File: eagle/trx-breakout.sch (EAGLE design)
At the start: 17 parts, among them J1 DF12NB(3.0)-10DX-0.5VHRS_DF12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, Q1 BSS84, Q2 BSS84, Q3 BSS123, Q4 BSS123

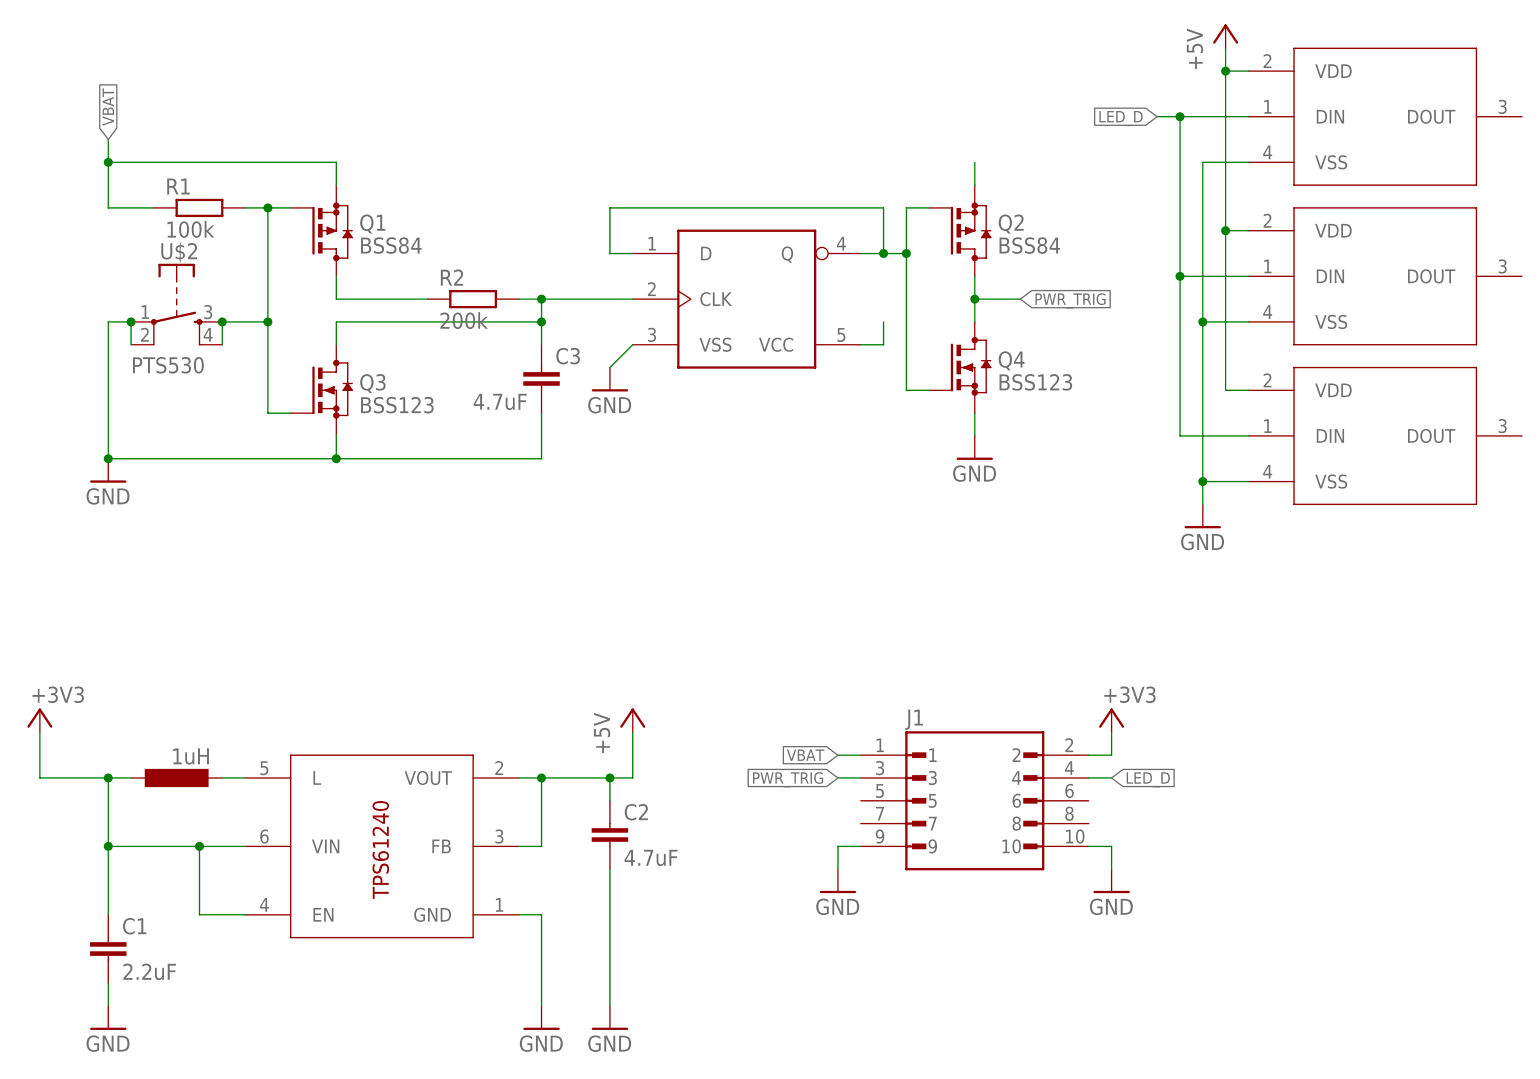
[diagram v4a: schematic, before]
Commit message: Designed new boards wit fixed errors
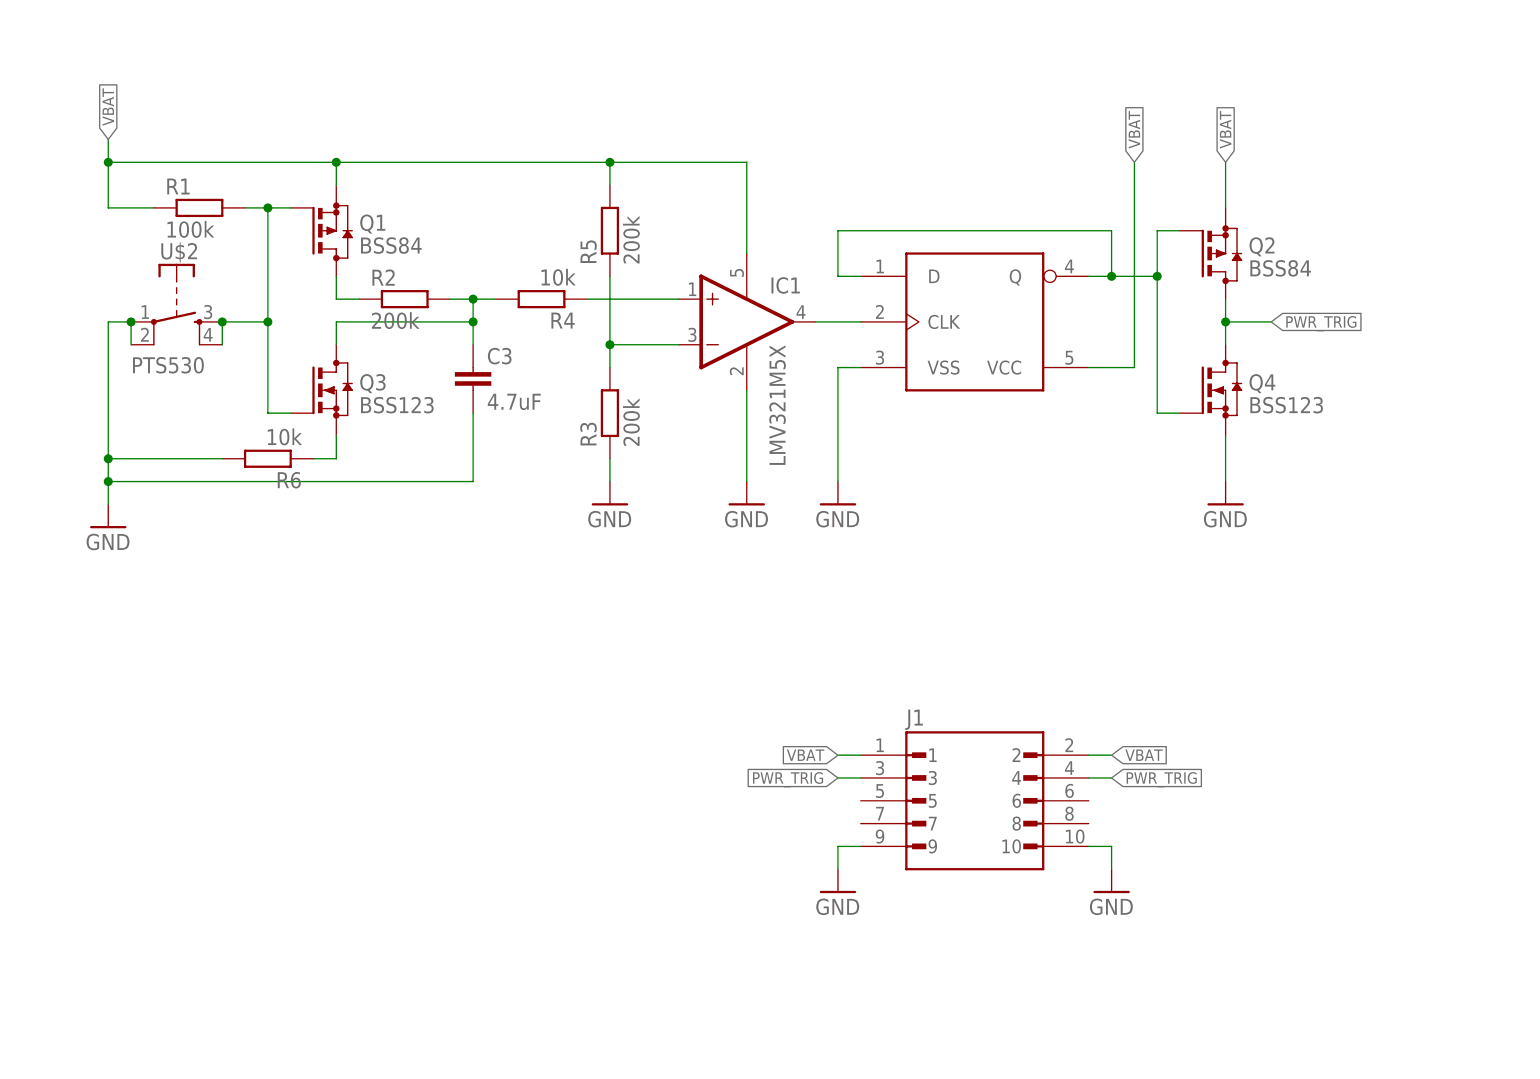
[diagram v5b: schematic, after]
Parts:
- removed C1: 2.2uF, rcl:C-EUC0805
- removed C2: 4.7uF, rcl:C-EUC0805
- removed U$3: TPS61240, texas-instruments:TPS61240
- removed U$4: 1uH, inductor-vishay:IHLP-1212
- removed U$5, U$6, U$7: ARGB_LED, led:ARGB_LED
- added IC1: LMV321M5X, linear:LMV321M5X
- added R3, R5: 200k, rcl:R-EU_R0805
- added R4, R6: 10k, rcl:R-EU_R0805
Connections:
- removed net +3V3: C1.1, J1.2, U$3.EN, U$3.VIN, U$4.1
- removed net +5V: C2.1, U$3.FB, U$3.VOUT, U$5.VDD, U$6.VDD, U$7.VDD
- removed net LED_D: J1.4, U$5.DIN, U$6.DIN, U$7.DIN
- new net N$8: Q3.S, R6.1
- net GND: now also IC1.V-, R3.1, R6.2; no longer C1.2, C2.2, Q3.S, U$3.GND, U$5.VSS, U$6.VSS, U$7.VSS
- net N$1: now also IC1.-IN, R3.2, R5.1; no longer U$3.L, U$4.2
- net N$3: now also R4.2; no longer U$1.CLK
- net N$6: now also IC1.+IN, R4.1; no longer U$1.VCC
- net N$7: now also IC1.OUT, U$1.CLK; no longer Q2.S
- net PWR_TRIG: now also J1.4
- net VBAT: now also IC1.V+, J1.2, Q2.S, R5.2, U$1.VCC
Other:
- moved on the sheet: C3, Q2, Q4, R2

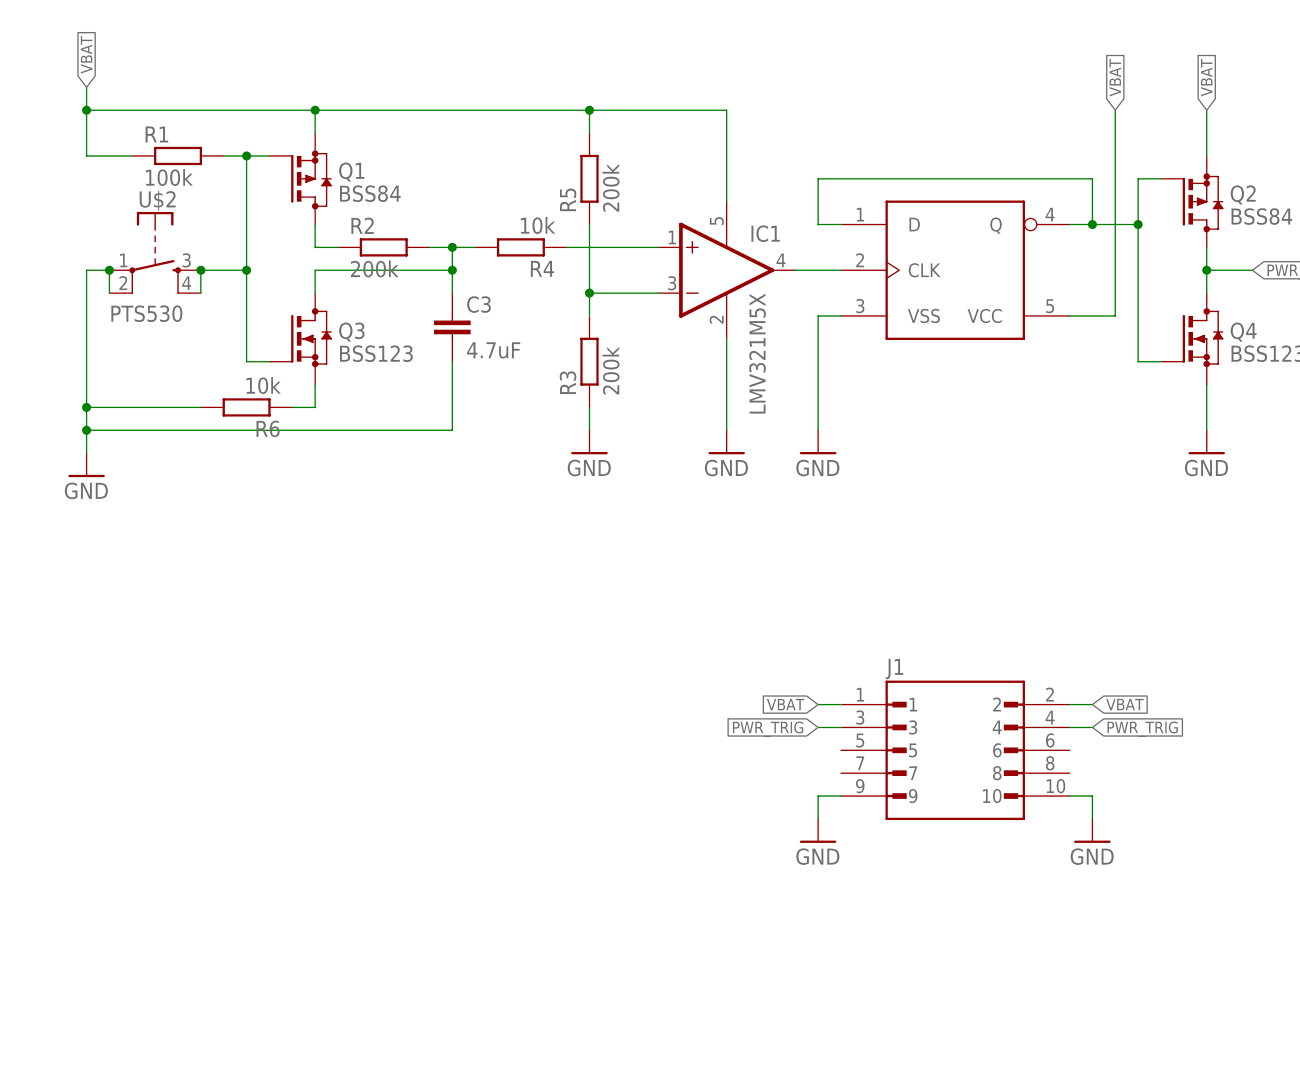
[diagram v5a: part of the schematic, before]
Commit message: Reworked breakout board
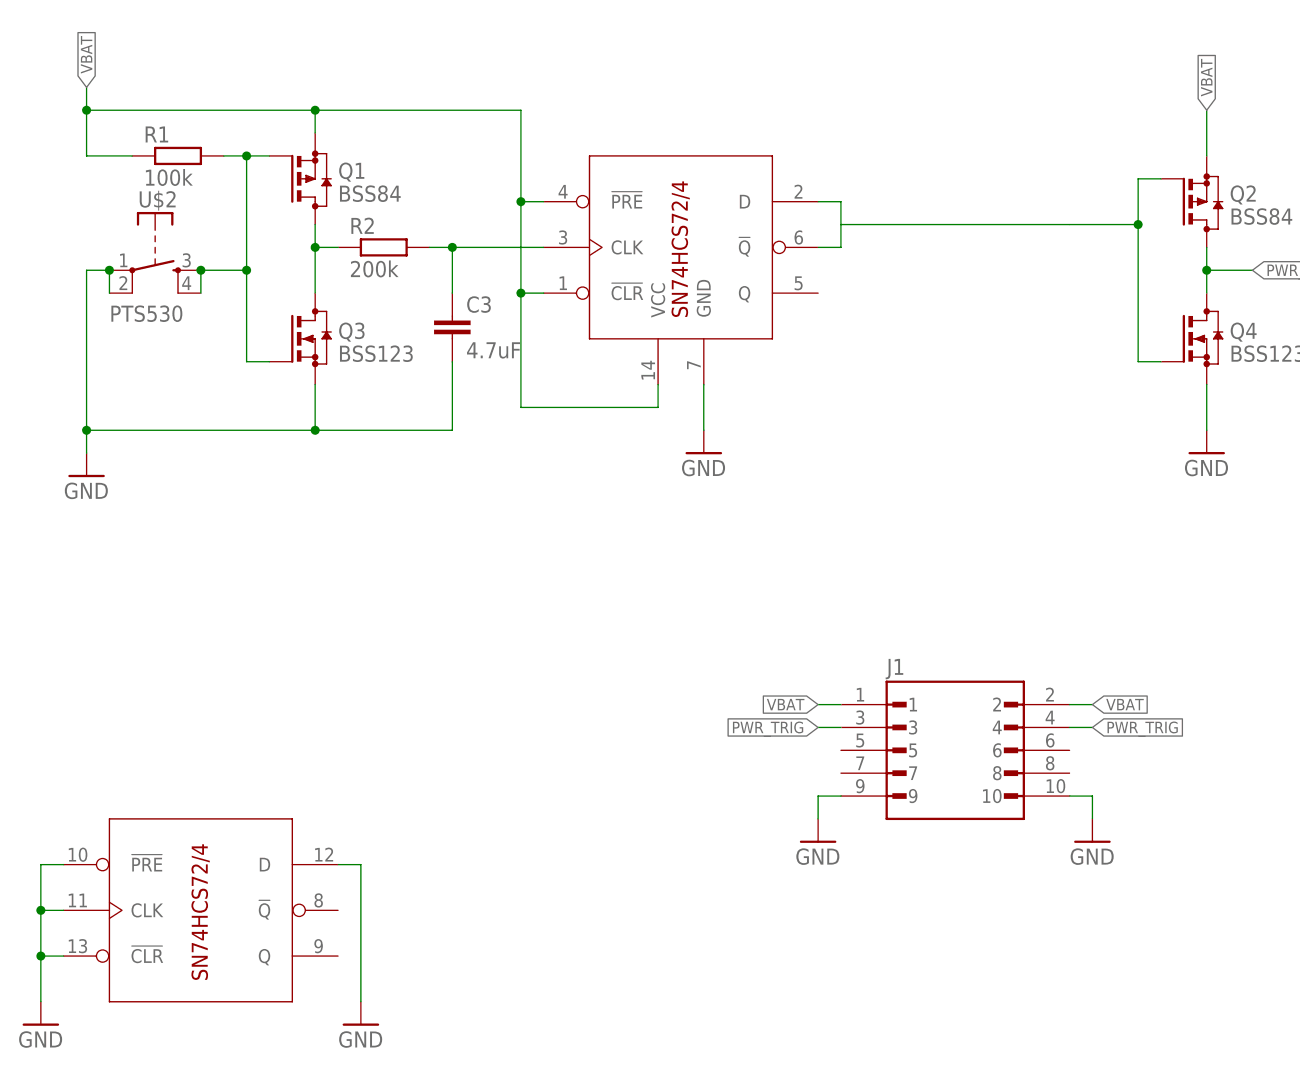
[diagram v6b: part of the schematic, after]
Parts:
- removed IC1: LMV321M5X, linear:LMV321M5X
- removed R3, R5: 200k, rcl:R-EU_R0805
- removed R4, R6: 10k, rcl:R-EU_R0805
- U$1: value SN74LVC1G80 -> SN74HCS72/4; device texas-instruments:SN74LVC1G80 -> texas-instruments:SN74HCS72/4
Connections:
- removed net N$6: IC1.+IN, R4.1
- removed net N$7: IC1.OUT, U$1.CLK
- removed net N$8: Q3.S, R6.1
- net GND: now also Q3.S, U$1G2.!CLR, U$1G2.!PRE, U$1G2.CLK, U$1G2.D, U$1SUPPPLY.GND; no longer IC1.V-, R3.1, R6.2, U$1.VSS
- net N$1: now also Q1.D, Q3.D, R2.1; no longer IC1.-IN, R3.2, R5.1
- net N$2: now also U$1G1.!Q, U$1G1.D; no longer Q1.D, R2.1
- net N$3: now also U$1G1.CLK; no longer Q3.D, R4.2
- net N$5: no longer U$1.D, U$1.Q
- net VBAT: now also U$1G1.!CLR, U$1G1.!PRE, U$1SUPPPLY.VCC; no longer IC1.V+, R5.2, U$1.VCC

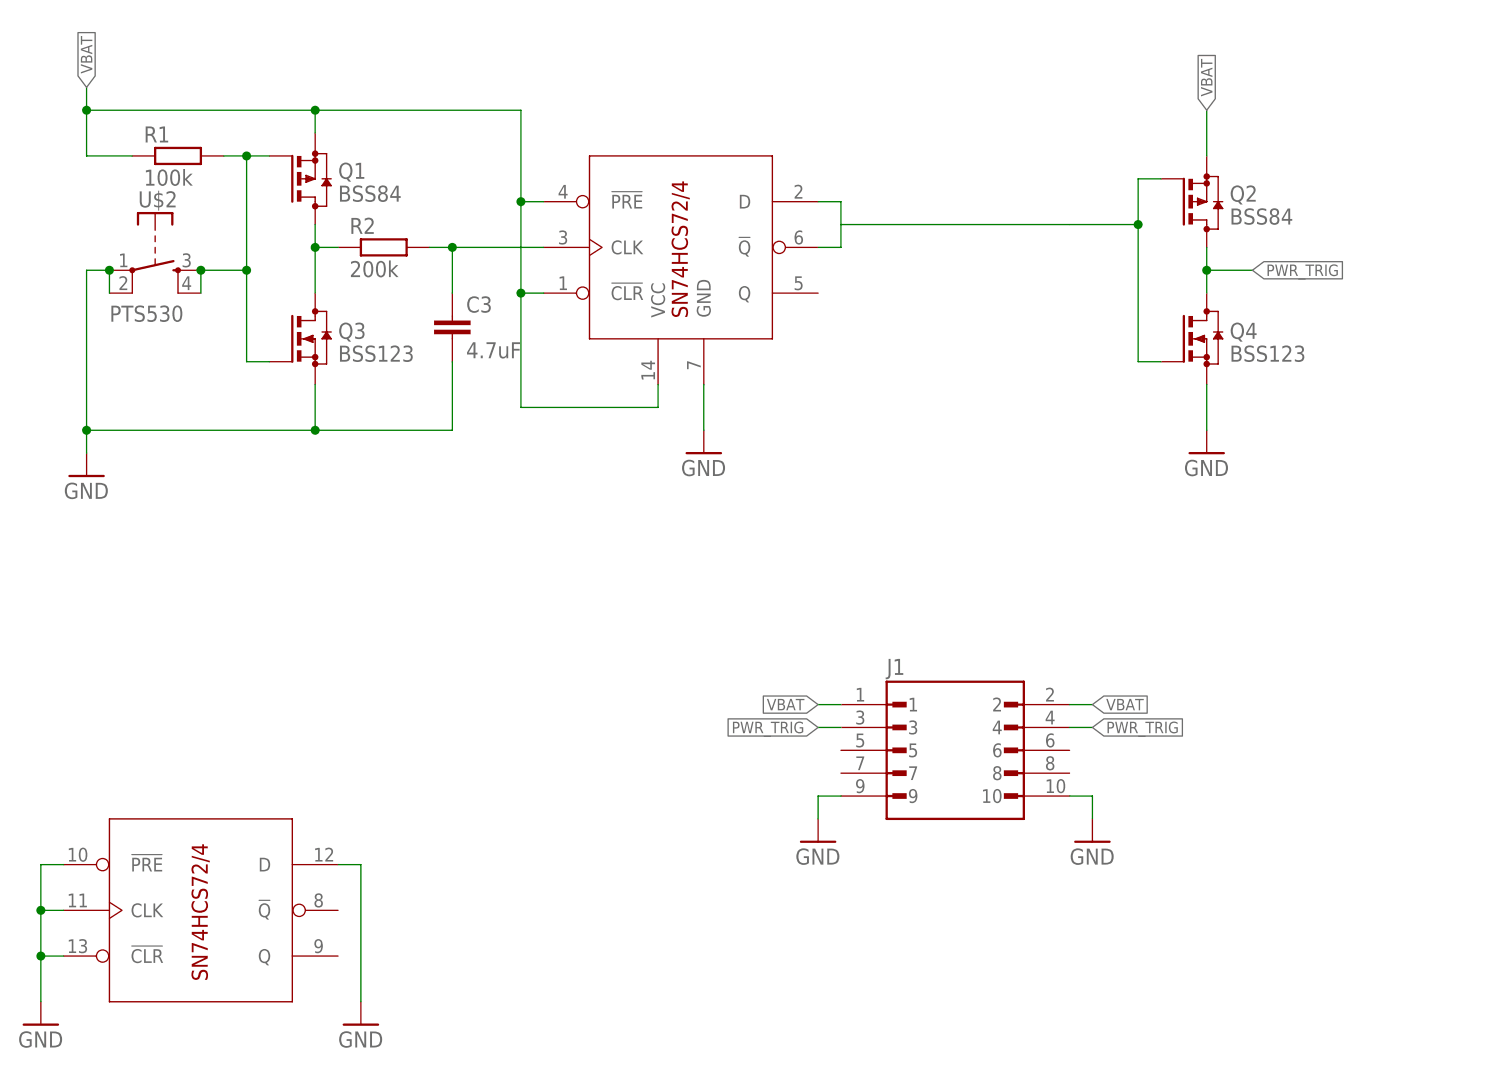
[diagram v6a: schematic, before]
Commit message: Modified board layout
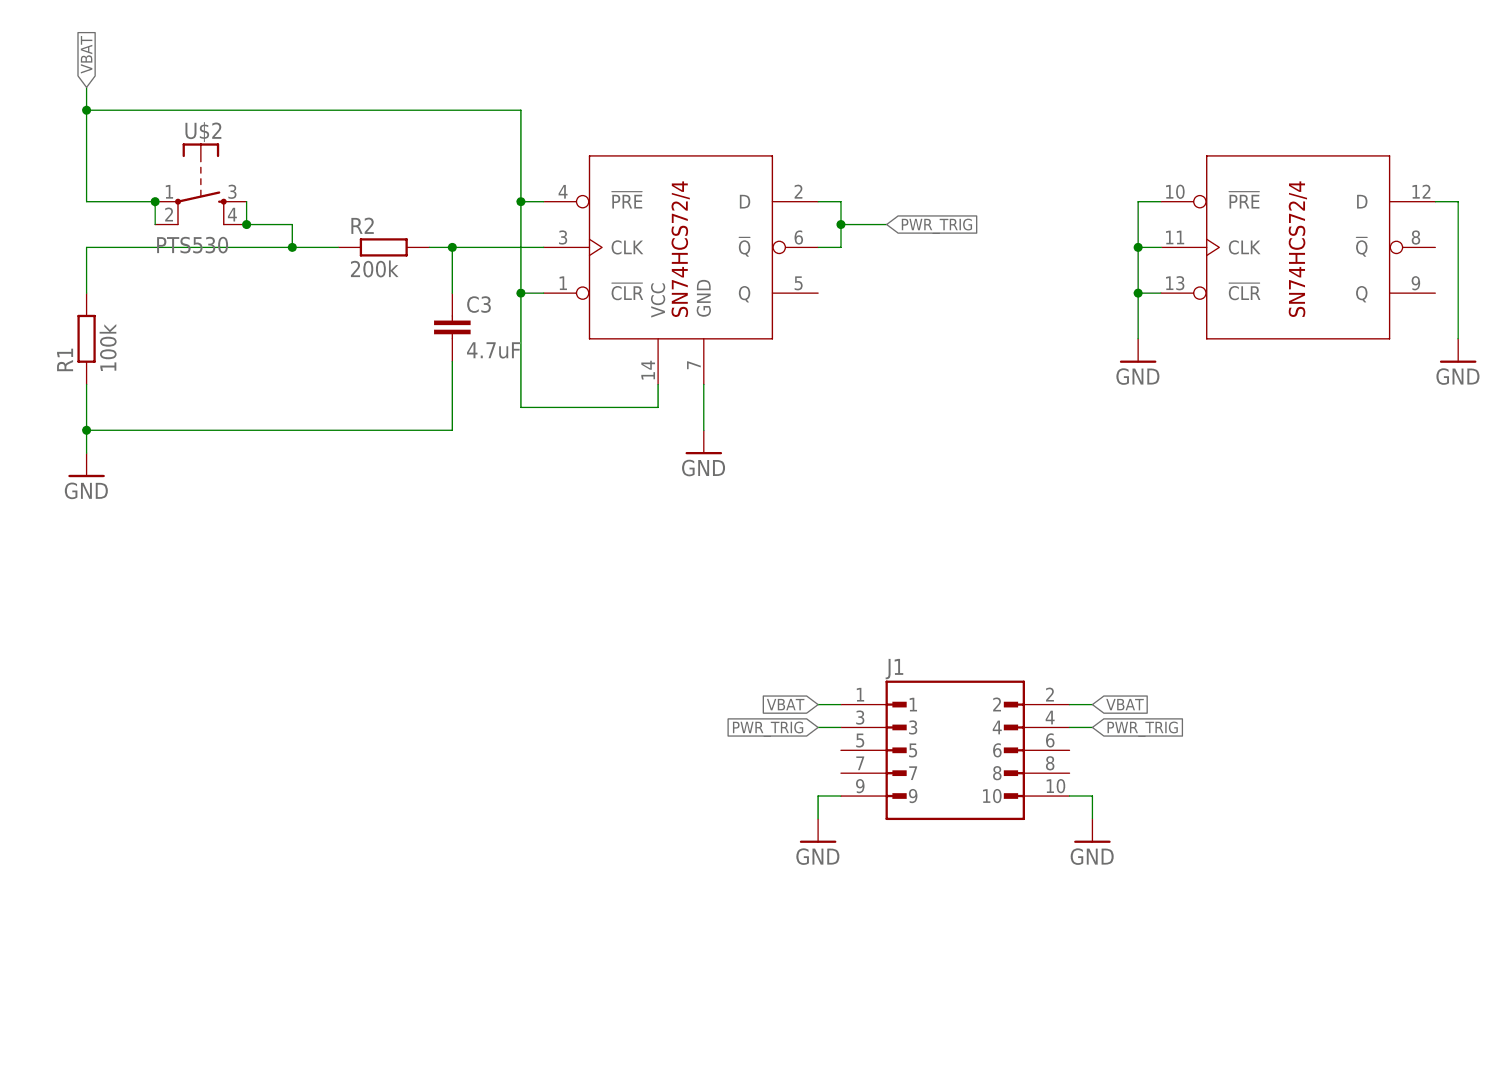
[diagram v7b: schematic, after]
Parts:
- removed Q1, Q2: BSS84, transistor-small-signal:BSS84
- removed Q3, Q4: BSS123, transistor-small-signal:BSS123
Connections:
- removed net N$1: Q1.D, Q3.D, R2.1
- removed net N$2: U$1G1.!Q, U$1G1.D
- removed net N$5: Q2.G, Q4.G
- net GND: now also R1.1; no longer Q3.S, Q4.S, U$2.P, U$2.P@1
- net N$4: now also R2.1; no longer Q1.G, Q3.G
- net PWR_TRIG: now also U$1G1.!Q, U$1G1.D; no longer Q2.D, Q4.D
- net VBAT: now also U$2.P, U$2.P@1; no longer Q1.S, Q2.S, R1.1
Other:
- moved on the sheet: R1, U$2
